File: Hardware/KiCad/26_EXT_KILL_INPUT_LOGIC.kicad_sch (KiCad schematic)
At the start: 0 parts

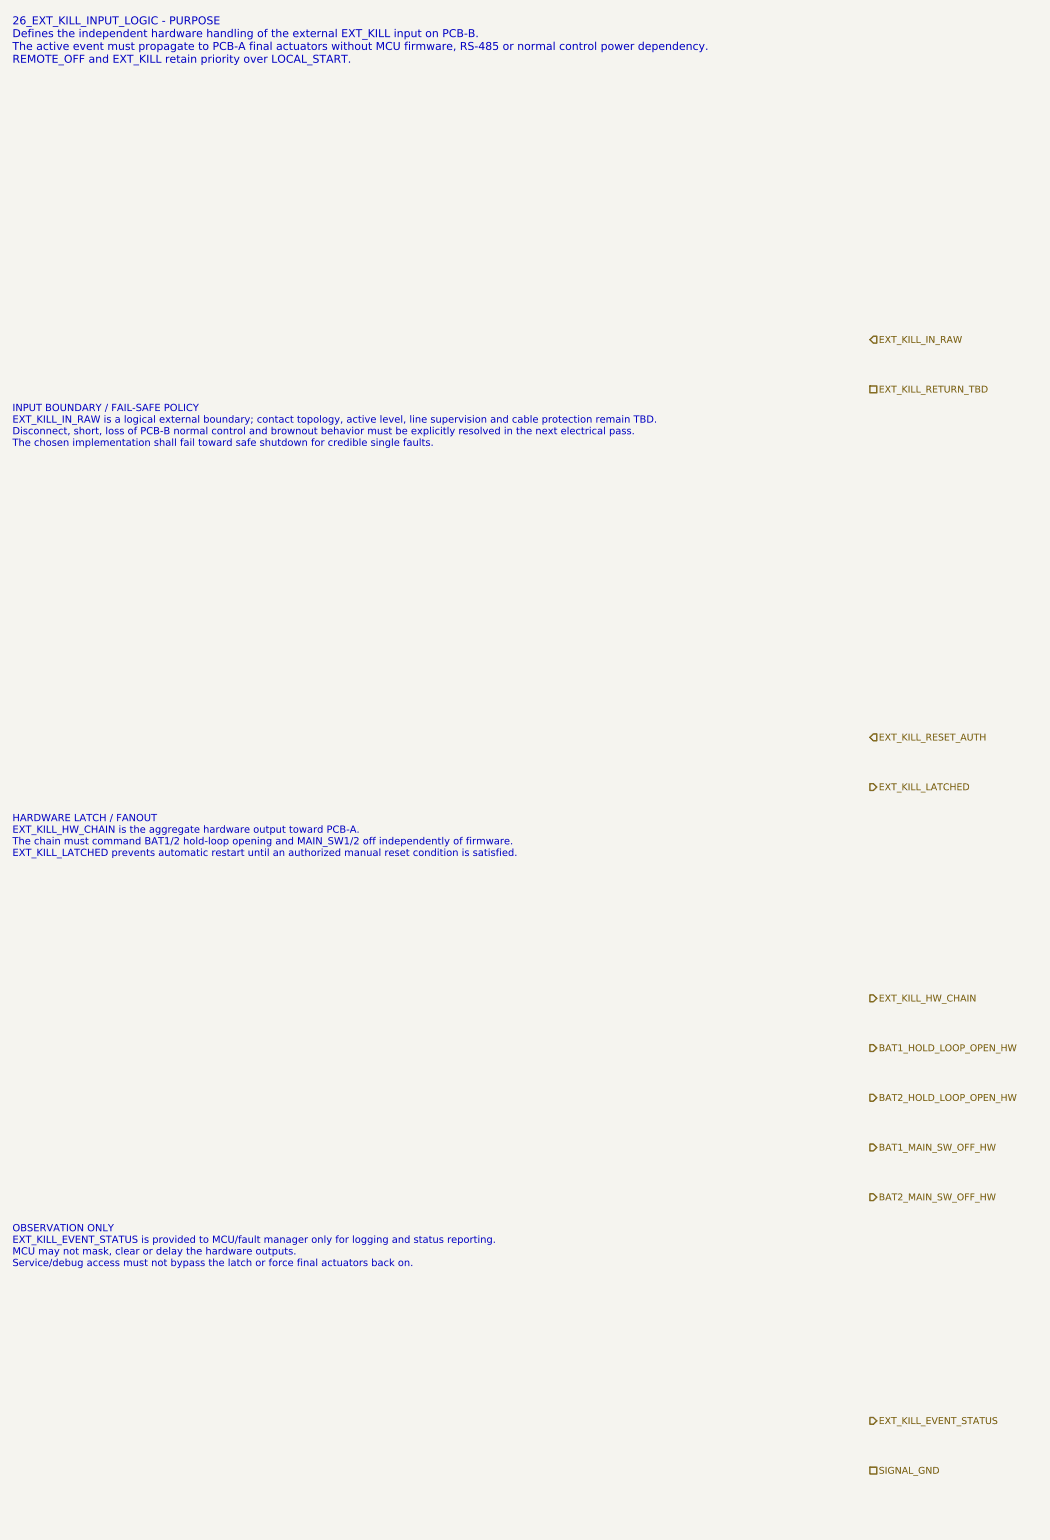
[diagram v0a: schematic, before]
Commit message: hardware: complete EXT_KILL event fanout interfaces
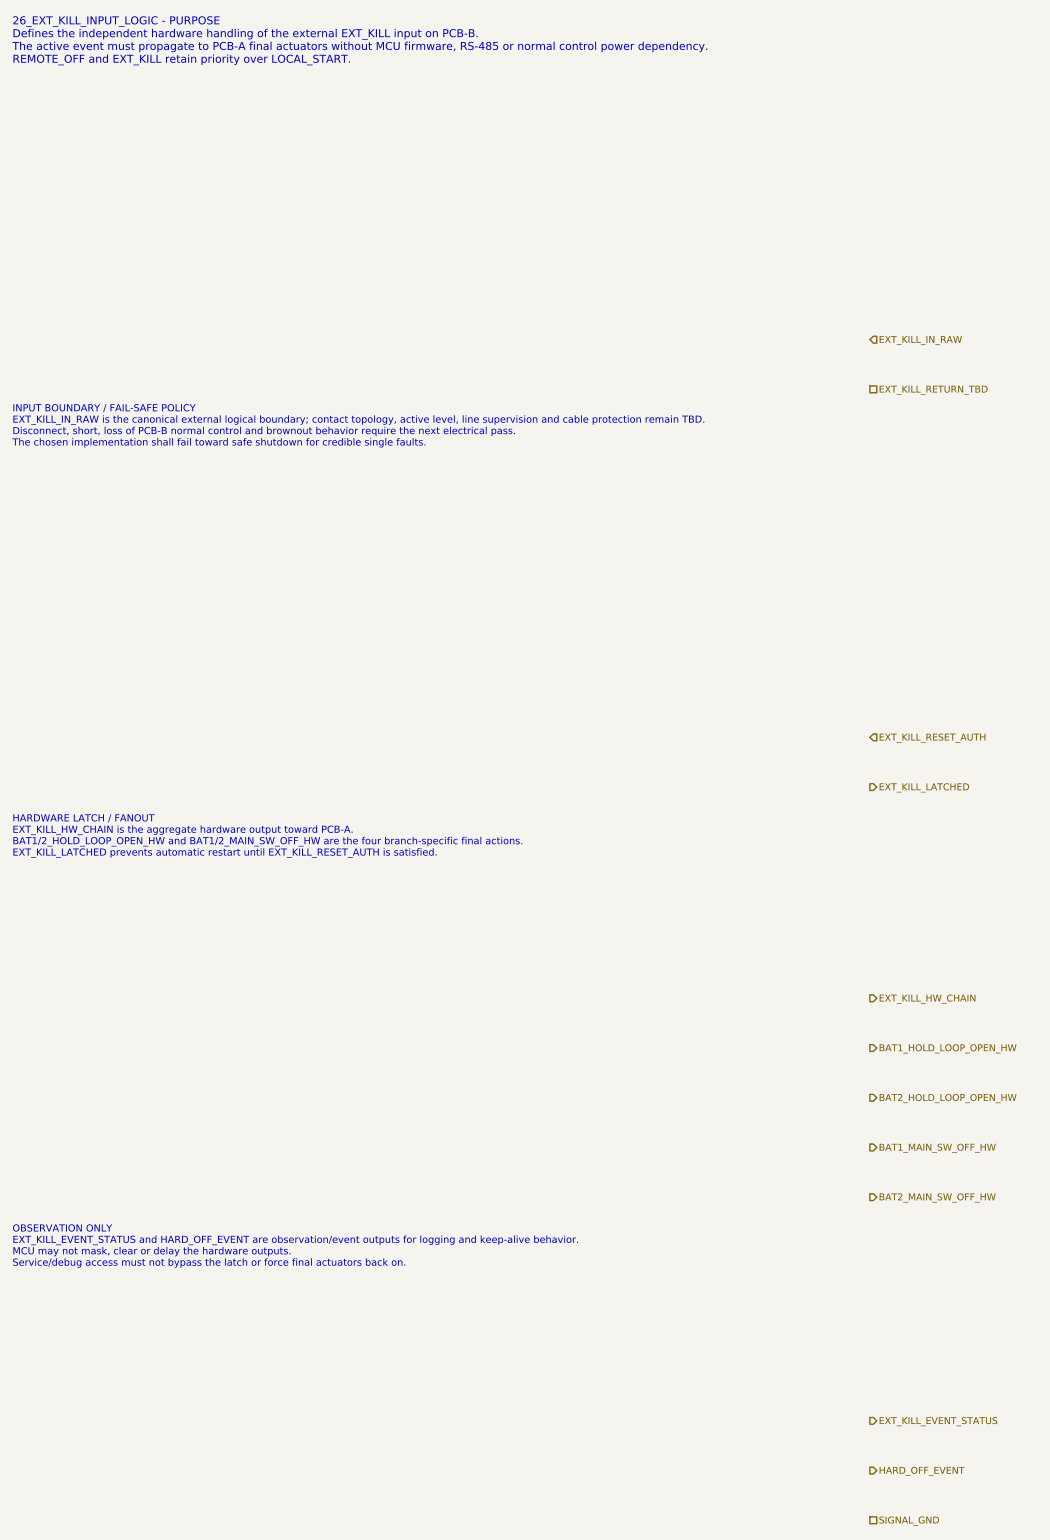
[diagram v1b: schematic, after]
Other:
- note added: "HARDWARE LATCH / FANOUT EXT_KILL_HW_CHAIN is the aggregate hardware output toward PCB-A. BAT1/2_HOLD_LOOP_OPEN_HW and BAT1/2_MAIN_SW_OFF_HW are the four branch-specific final actions. EXT_KILL_LATCHED prevents automatic restart until EXT_KILL_RESET_AUTH is satisfied."
- note added: "INPUT BOUNDARY / FAIL-SAFE POLICY EXT_KILL_IN_RAW is the canonical external logical boundary; contact topology, active level, line supervision and cable protection remain TBD. Disconnect, short, loss of PCB-B normal control and brownout behavior require the next electrical pass. The chosen implementation shall fail toward safe shutdown for credible single faults."
- note added: "OBSERVATION ONLY EXT_KILL_EVENT_STATUS and HARD_OFF_EVENT are observation/event outputs for logging and keep-alive behavior. MCU may not mask, clear or delay the hardware outputs. Service/debug access must not bypass the latch or force final actuators back on."
- note removed: "HARDWARE LATCH / FANOUT EXT_KILL_HW_CHAIN is the aggregate hardware output toward PCB-A. The chain must command BAT1/2 hold-loop opening and MAIN_SW1/2 off independently of firmware. EXT_KILL_LATCHED prevents automatic restart until an authorized manual reset condition is satisfied."
- note removed: "INPUT BOUNDARY / FAIL-SAFE POLICY EXT_KILL_IN_RAW is a logical external boundary; contact topology, active level, line supervision and cable protection remain TBD. Disconnect, short, loss of PCB-B normal control and brownout behavior must be explicitly resolved in the next electrical pass. The chosen implementation shall fail toward safe shutdown for credible single faults."
- note removed: "OBSERVATION ONLY EXT_KILL_EVENT_STATUS is provided to MCU/fault manager only for logging and status reporting. MCU may not mask, clear or delay the hardware outputs. Service/debug access must not bypass the latch or force final actuators back on."
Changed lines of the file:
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@@
 		(title "26_EXT_KILL_INPUT_LOGIC - independent emergency shutdown chain")
 		(date "2026-07-15")
-		(rev "B0")
+		(rev "B1")
 		(company "Gonoboben/plataVM")
-		(comment 1 "Architecture Level A/B: external EXT_KILL boundary, latch and hardware fanout")
+		(comment 1 "Interface consistency: external input, latch, final actions and HARD_OFF event")
 		(comment 2 "Text-only placeholders; no switch, relay, optocoupler, comparator, latch, connector or footprint selected")
 	)
@@
 		(uuid "ctrl-reserve-00000026-0000-4000-8000-000000000101")
 	)
-	(text "INPUT BOUNDARY / FAIL-SAFE POLICY\nEXT_KILL_IN_RAW is a logical external boundary; contact topology, active level, line supervision and cable protection remain TBD.\nDisconnect, short, loss of PCB-B normal control and brownout behavior must be explicitly resolved in the next electrical pass.\nThe chosen implementation shall fail toward safe shutdown for credible single faults."
+	(text "INPUT BOUNDARY / FAIL-SAFE POLICY\nEXT_KILL_IN_RAW is the canonical external logical boundary; contact topology, active level, line supervision and cable protection remain TBD.\nDisconnect, short, loss of PCB-B normal control and brownout behavior require the next electrical pass.\nThe chosen implementation shall fail toward safe shutdown for credible single faults."
 		(exclude_from_sim no)
 		(at 12 76 0)
-		(effects (font (size 1.16 1.16)) (justify left))
+		(effects (font (size 1.14 1.14)) (justify left))
 		(uuid "ctrl-reserve-00000026-0000-4000-8000-000000000102")
 	)
-	(text "HARDWARE LATCH / FANOUT\nEXT_KILL_HW_CHAIN is the aggregate hardware output toward PCB-A.\nThe chain must command BAT1/2 hold-loop opening and MAIN_SW1/2 off independently of firmware.\nEXT_KILL_LATCHED prevents automatic restart until an authorized manual reset condition is satisfied."
+	(text "HARDWARE LATCH / FANOUT\nEXT_KILL_HW_CHAIN is the aggregate hardware output toward PCB-A.\nBAT1/2_HOLD_LOOP_OPEN_HW and BAT1/2_MAIN_SW_OFF_HW are the four branch-specific final actions.\nEXT_KILL_LATCHED prevents automatic restart until EXT_KILL_RESET_AUTH is satisfied."
 		(exclude_from_sim no)
 		(at 12 142 0)
-		(effects (font (size 1.16 1.16)) (justify left))
+		(effects (font (size 1.14 1.14)) (justify left))
 		(uuid "ctrl-reserve-00000026-0000-4000-8000-000000000103")
 	)
-	(text "OBSERVATION ONLY\nEXT_KILL_EVENT_STATUS is provided to MCU/fault manager only for logging and status reporting.\nMCU may not mask, clear or delay the hardware outputs.\nService/debug access must not bypass the latch or force final actuators back on."
+	(text "OBSERVATION ONLY\nEXT_KILL_EVENT_STATUS and HARD_OFF_EVENT are observation/event outputs for logging and keep-alive behavior.\nMCU may not mask, clear or delay the hardware outputs.\nService/debug access must not bypass the latch or force final actuators back on."
 		(exclude_from_sim no)
 		(at 12 208 0)
-		(effects (font (size 1.16 1.16)) (justify left))
+		(effects (font (size 1.14 1.14)) (justify left))
 		(uuid "ctrl-reserve-00000026-0000-4000-8000-000000000104")
 	)
@@
 	(hierarchical_label "BAT2_MAIN_SW_OFF_HW" (shape output) (exclude_from_sim no) (at 150 200 0) (effects (font (size 1.1 1.1)) (justify left)) (uuid "ctrl-reserve-00000026-0000-4000-8000-000000000209"))
 	(hierarchical_label "EXT_KILL_EVENT_STATUS" (shape output) (exclude_from_sim no) (at 150 236 0) (effects (font (size 1.1 1.1)) (justify left)) (uuid "ctrl-reserve-00000026-0000-4000-8000-000000000210"))
-	(hierarchical_label "SIGNAL_GND" (shape passive) (exclude_from_sim no) (at 150 244 0) (effects (font (size 1.1 1.1)) (justify left)) (uuid "ctrl-reserve-00000026-0000-4000-8000-000000000211"))
+	(hierarchical_label "HARD_OFF_EVENT" (shape output) (exclude_from_sim no) (at 150 244 0) (effects (font (size 1.1 1.1)) (justify left)) (uuid "ctrl-reserve-00000026-0000-4000-8000-000000000212"))
+	(hierarchical_label "SIGNAL_GND" (shape passive) (exclude_from_sim no) (at 150 252 0) (effects (font (size 1.1 1.1)) (justify left)) (uuid "ctrl-reserve-00000026-0000-4000-8000-000000000211"))
 )
